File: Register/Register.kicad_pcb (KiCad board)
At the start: 2 copper layers, 99.6 x 59.9 mm, 22 parts, among them J1 Conn_01x16, J2 Conn_01x16, J3 Conn_01x08, J4 Conn_01x08, J5 Conn_01x12, U1 SN74LS04N, U2 74LS173, U3 74LS173, U4 74LS245

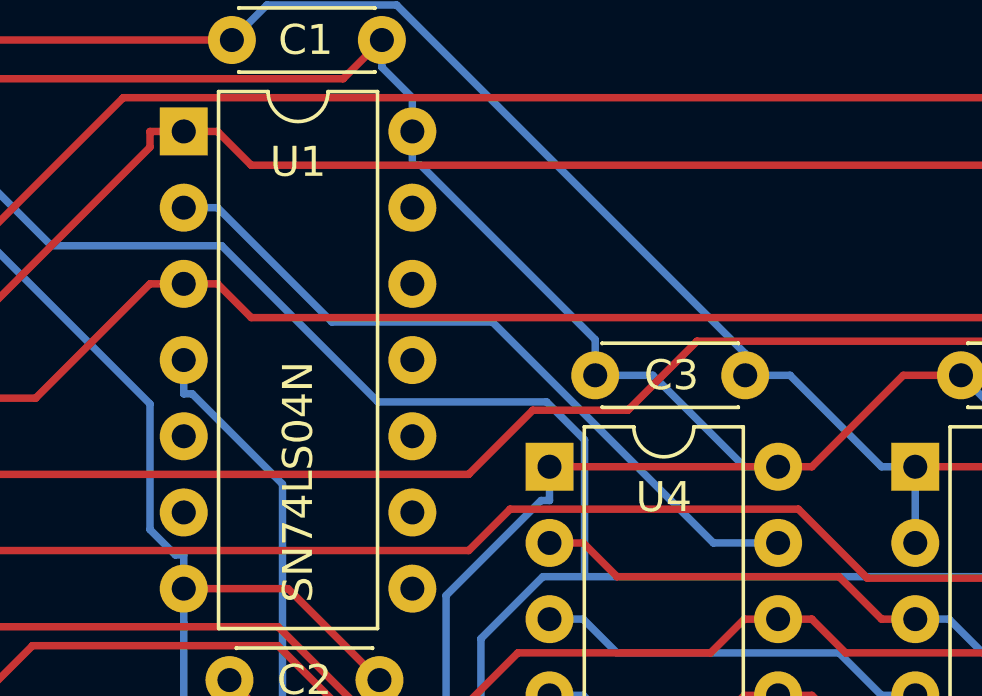
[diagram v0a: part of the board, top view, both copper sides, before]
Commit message: Fixed floating inputs; improved power; added parts list; replaced JK latches
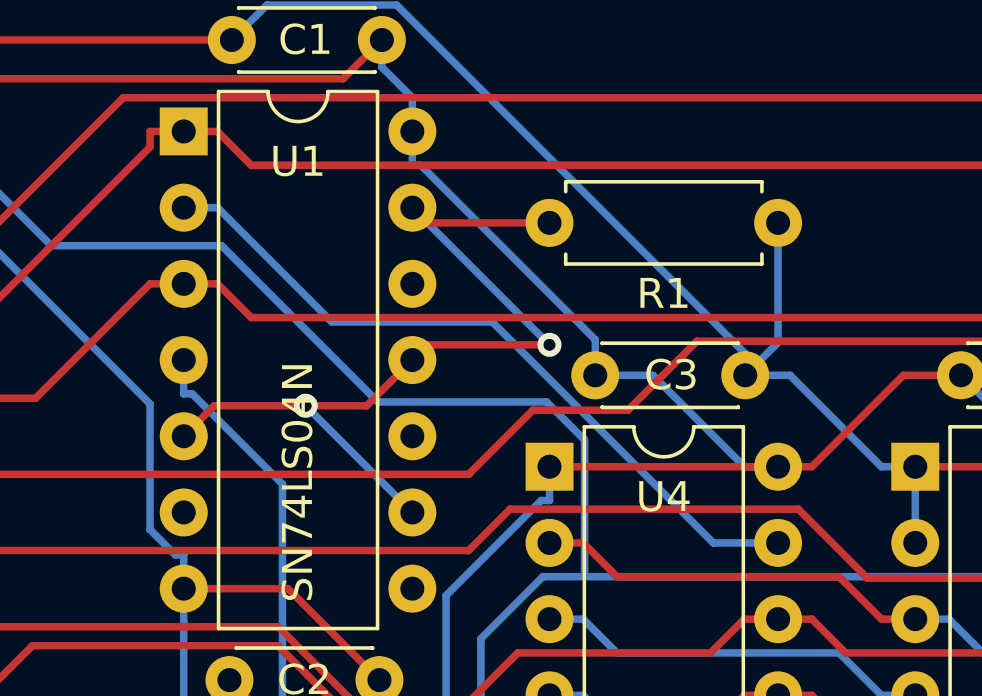
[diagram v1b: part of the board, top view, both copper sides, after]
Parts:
- added R1: 10k, Resistor_THT:R_Axial_DIN0207_L6.3mm_D2.5mm_P7.62mm_Horizontal, F.Cu at (98.6, 66.0)
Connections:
- U1 pad 11: Net-(U1-Pad11) -> Net-(R1-Pad2)
- U1 pad 13: Net-(U1-Pad13) -> Net-(R1-Pad2)
- U1 pad 5: Net-(U1-Pad5) -> Net-(R1-Pad2)
- U1 pad 9: Net-(U1-Pad9) -> Net-(R1-Pad2)
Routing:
- net Net-(R1-Pad2): track 0.00 -> 29.7 mm, vias 0 -> 2
- net GND: track 217.8 -> 223.4 mm
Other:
- rule pad_to_mask_clearance: 0.051 -> 0

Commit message: Update all boards to r3, and update revision log and gitignore
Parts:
- added HOLE1: MountingHole_2.2mm_M2_DIN965_Pad, MountingHole:MountingHole_2.2mm_M2_DIN965_Pad, F.Cu at (70.6, 52.3)
- added HOLE2: MountingHole_2.2mm_M2_DIN965_Pad, MountingHole:MountingHole_2.2mm_M2_DIN965_Pad, F.Cu at (162.1, 52.3)
- added HOLE3: MountingHole_2.2mm_M2_DIN965_Pad, MountingHole:MountingHole_2.2mm_M2_DIN965_Pad, F.Cu at (70.6, 104.1)
- added HOLE4: MountingHole_2.2mm_M2_DIN965_Pad, MountingHole:MountingHole_2.2mm_M2_DIN965_Pad, F.Cu at (162.1, 104.1)
- U1: value SN74LS04N -> SN74HC04N
- U2, U3: value 74LS173 -> 74HC173
- U4: value 74LS245 -> 74HC245
- moved J5 27.9 mm to (150.3, 74.2), turned to -90 degrees
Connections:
- net ~SIG_IN renamed ~{SIG_IN}
- net ~SIG_OUT renamed ~{SIG_OUT}
- D1 pad 2: R0 -> R7
- D2 pad 2: R1 -> R6
- D3 pad 2: R2 -> R5
- D4 pad 2: R3 -> R4
- D5 pad 2: R4 -> R3
- D6 pad 2: R5 -> R2
- D7 pad 2: R6 -> R1
- D8 pad 2: R7 -> R0
- U1 pad 10: Net-(U1-Pad10) -> unconnected-(U1-5Y-Pad10)
- U1 pad 12: Net-(U1-Pad12) -> unconnected-(U1-6Y-Pad12)
- U1 pad 6: Net-(U1-Pad6) -> unconnected-(U1-3Y-Pad6)
- U1 pad 8: Net-(U1-Pad8) -> unconnected-(U1-4Y-Pad8)
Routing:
- net R0: track 84.7 -> 124.4 mm
- net R7: track 133.5 -> 96.6 mm, vias 0 -> 1
- net BUS3: track 127.2 -> 95.3 mm, vias 2 -> 1
- net R1: track 97.3 -> 125.0 mm
- net BUS4: track 117.1 -> 94.6 mm
- net R3: track 101.4 -> 120.3 mm
- net R6: track 120.2 -> 104.1 mm
- net R4: track 112.6 -> 128.4 mm
- net RESET: track 125.9 -> 138.0 mm, vias 0 -> 1
- net CLOCK: track 164.6 -> 153.4 mm, vias 0 -> 1
- net R2: track 101.4 -> 111.4 mm, vias 0 -> 1
- net R5: track 115.7 -> 125.6 mm, vias 0 -> 1
- net GND: track 223.4 -> 231.8 mm
- net SIG_OUT: track 97.0 -> 104.1 mm
- net VCC: track 139.0 -> 144.1 mm
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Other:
- net class Default removed
